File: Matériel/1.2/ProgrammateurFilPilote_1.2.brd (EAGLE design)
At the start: 85.5 x 66.8 mm, 76 parts, among them IC2 MCP23017, P1 PADSMALL, P2 PADSMALL, T1 2N2222

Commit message: Màj v1.2
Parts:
- removed CONTACT_SEC: (no value), con-ptr500:AK500/2
- added J2: GROVE-I2C, seeed-opl-Connector:4P-2.0
- added RL: (no value), con-ptr500:AK500/2
- added SW1: HLS8L-DC5V-S-C, seeed-opl-Connector:5P-L19.0XW15.0XH15.0MM
- D1, D10, D11, D12, D13, D14, D2, D3, D4, D5, D6, D7, D8, D9: value CGRM4001-G -> SL1J; device diode:SOD-123_MINI-SMA -> seeed-opl-Discrete:DO-214AC
- moved 230V 34.0 mm to (5.41, 21.0)
- moved F1 33.8 mm to (15.2, 23.6), turned to 0 degrees
- moved T1 14.2 mm to (21.8, 2.00)
- moved D1 12.7 mm to (16.3, 60.7), turned to 0 degrees
- moved D9 12.7 mm to (16.3, 40.4), turned to 0 degrees
- moved D11 12.7 mm to (16.3, 35.3), turned to 0 degrees
- moved D3 12.7 mm to (16.3, 55.6), turned to 0 degrees
- moved D5 12.7 mm to (16.3, 50.5), turned to 0 degrees
- moved D7 12.7 mm to (16.3, 45.5), turned to 0 degrees
- moved D13 12.6 mm to (16.3, 30.2), turned to 0 degrees
- moved FILPILOTE 11.4 mm to (5.41, 43.7)
- moved D12 10.2 mm to (16.3, 32.8), turned to 0 degrees
- moved D2 10.2 mm to (16.3, 58.2), turned to 0 degrees
- moved D4 10.2 mm to (16.3, 53.1), turned to 0 degrees
- moved D6 10.2 mm to (16.3, 48.0), turned to 0 degrees
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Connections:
- removed net N$17: 230V.2, F1.1
- removed net N$18: CONTACT_SEC.2, RELAIS.5
- removed net N$20: CONTACT_SEC.1, RELAIS.7
- removed net NEUTRE: 230V.1
- new net COM: RELAIS.7, RL.1, SW1.1
- new net N$16: 230V.1, F1.1
- new net NF: RL.2, SW1.5
- new net NO: 230V.2, RELAIS.5, SW1.4
- net +3V3: now also J2.2
- net +5V: now also SW1.2
- net FP1: now also D1.1, D2.2; no longer D1.A, D2.C
- net FP2: now also D3.1, D4.2; no longer D3.A, D4.C
- net FP3: now also D5.1, D6.2; no longer D5.A, D6.C
- net FP4: now also D7.1, D8.2; no longer D7.A, D8.C
- net FP5: now also D10.2, D9.1; no longer D10.C, D9.A
- net FP6: now also D11.1, D12.2; no longer D11.A, D12.C
- net FP7: now also D13.1, D14.1; no longer D13.A, D14.C
- net GND: now also J2.1
- net N$1: now also D1.2; no longer D1.C
- net N$15: now also SW1.3
- net N$2: now also D2.1; no longer D2.A
- net N$22: now also D3.2; no longer D3.C
- net N$24: now also D5.2; no longer D5.C
- net N$25: now also D4.1; no longer D4.A
- net N$26: now also D7.2; no longer D7.C
- net N$29: now also D6.1; no longer D6.A
- net N$31: now also D8.1; no longer D8.A
- net N$42: now also D9.2; no longer D9.C
- net N$49: now also D10.1; no longer D10.A
- net N$51: now also D12.1; no longer D12.A
- net S$1: now also D11.2; no longer D11.C
- net S$11: now also D14.2; no longer D14.A
- net S$3: now also D13.2; no longer D13.C
- net SCL: now also J2.4
- net SDA: now also J2.3
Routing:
- net COM: track 0.00 -> 30.3 mm
- net N$21: track 21.8 -> 39.5 mm, vias 0 -> 2
- net N$18: track 14.1 -> 0.00 mm
- net NO: track 0.00 -> 13.7 mm
- net SCL: track 117.2 -> 130.2 mm, vias 1 -> 2
- net PHASE: track 123.0 -> 111.3 mm
- net N$15: track 17.4 -> 28.2 mm
- net N$24: track 16.0 -> 6.10 mm
- net N$22: track 15.9 -> 6.10 mm
- net N$17: track 9.71 -> 0.00 mm
- net N$1: track 15.7 -> 6.10 mm
- net N$26: track 15.2 -> 6.10 mm
- net NF: track 0.00 -> 8.71 mm
- net SDA: track 123.3 -> 131.8 mm
- net N$42: track 14.4 -> 6.10 mm
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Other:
- board text added: "1,25A"
- board text added: "COM"
- board text added: "NF"
- board text added: "NO"
- board text added: "Programmateur Fil Pilote (v1.2 - 12/2014)"
- board text added: "Temporisé"
- board text removed: "CTC Sec"
- board text removed: "D'"
- board text removed: "Neutre"
- board text removed: "Programmateur Fil Pilote (v1.2 - 11/2014)"
- board text removed: "Temporisé 1,25A"
- board text removed: "~N"
- board text removed: "~P"

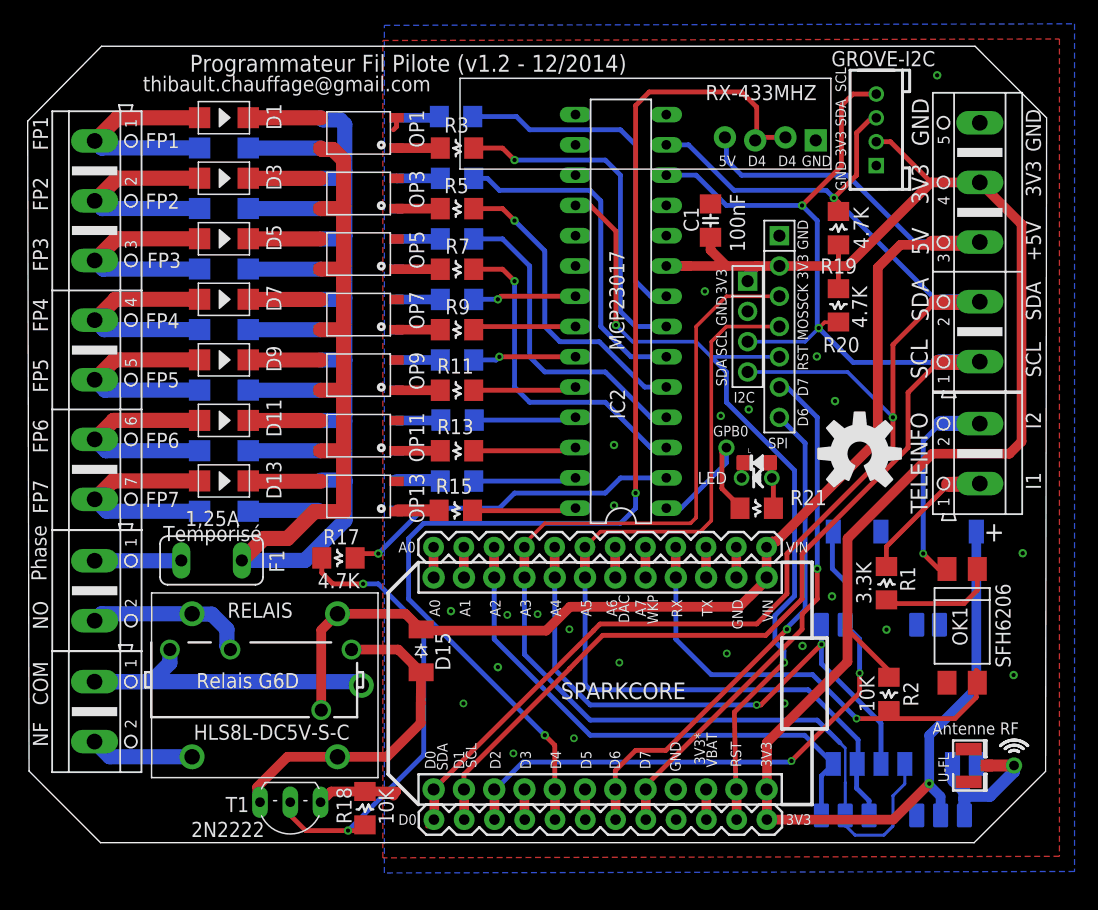
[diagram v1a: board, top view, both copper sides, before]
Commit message: Passage en Révision 1.2b
Correction d'inversion du sens du connecteur Grove
Correction d'inversion diode D14
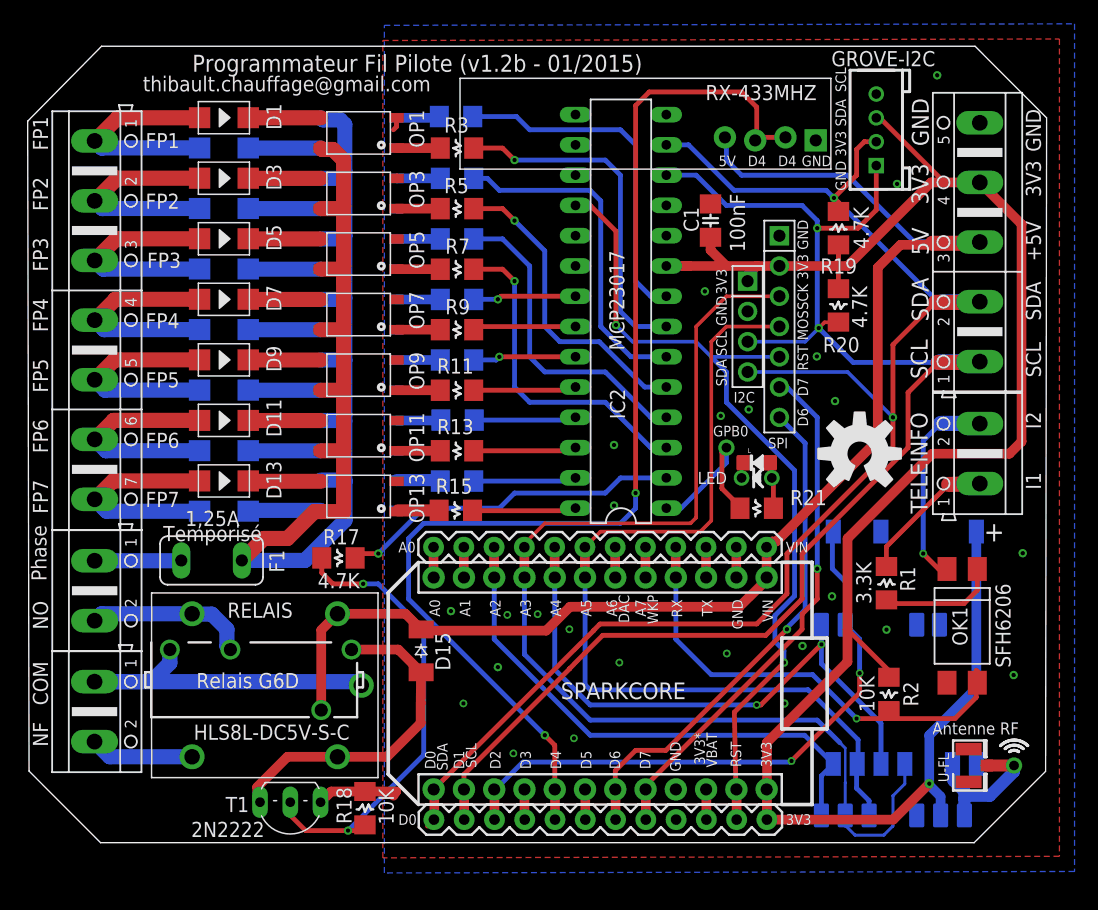
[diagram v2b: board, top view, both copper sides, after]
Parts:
- turned D14 to 0 degrees
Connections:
- net +3V3: now also J2.3; no longer J2.2
- net FP7: now also D14.2; no longer D14.1
- net GND: now also J2.4; no longer J2.1
- net S$11: now also D14.1; no longer D14.2
- net SCL: now also J2.1; no longer J2.4
- net SDA: now also J2.2; no longer J2.3
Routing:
- net SCL: track 130.2 -> 126.5 mm
- net +3V3: track 161.2 -> 163.2 mm
- net SDA: track 131.8 -> 130.1 mm
- net GND: vias 24 -> 25
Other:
- board text added: "Programmateur Fil Pilote (v1.2b - 01/2015)"
- board text removed: "Programmateur Fil Pilote (v1.2 - 12/2014)"
